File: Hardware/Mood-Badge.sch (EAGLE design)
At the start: 8 parts, among them U1 ATMEGA328P_TQFP

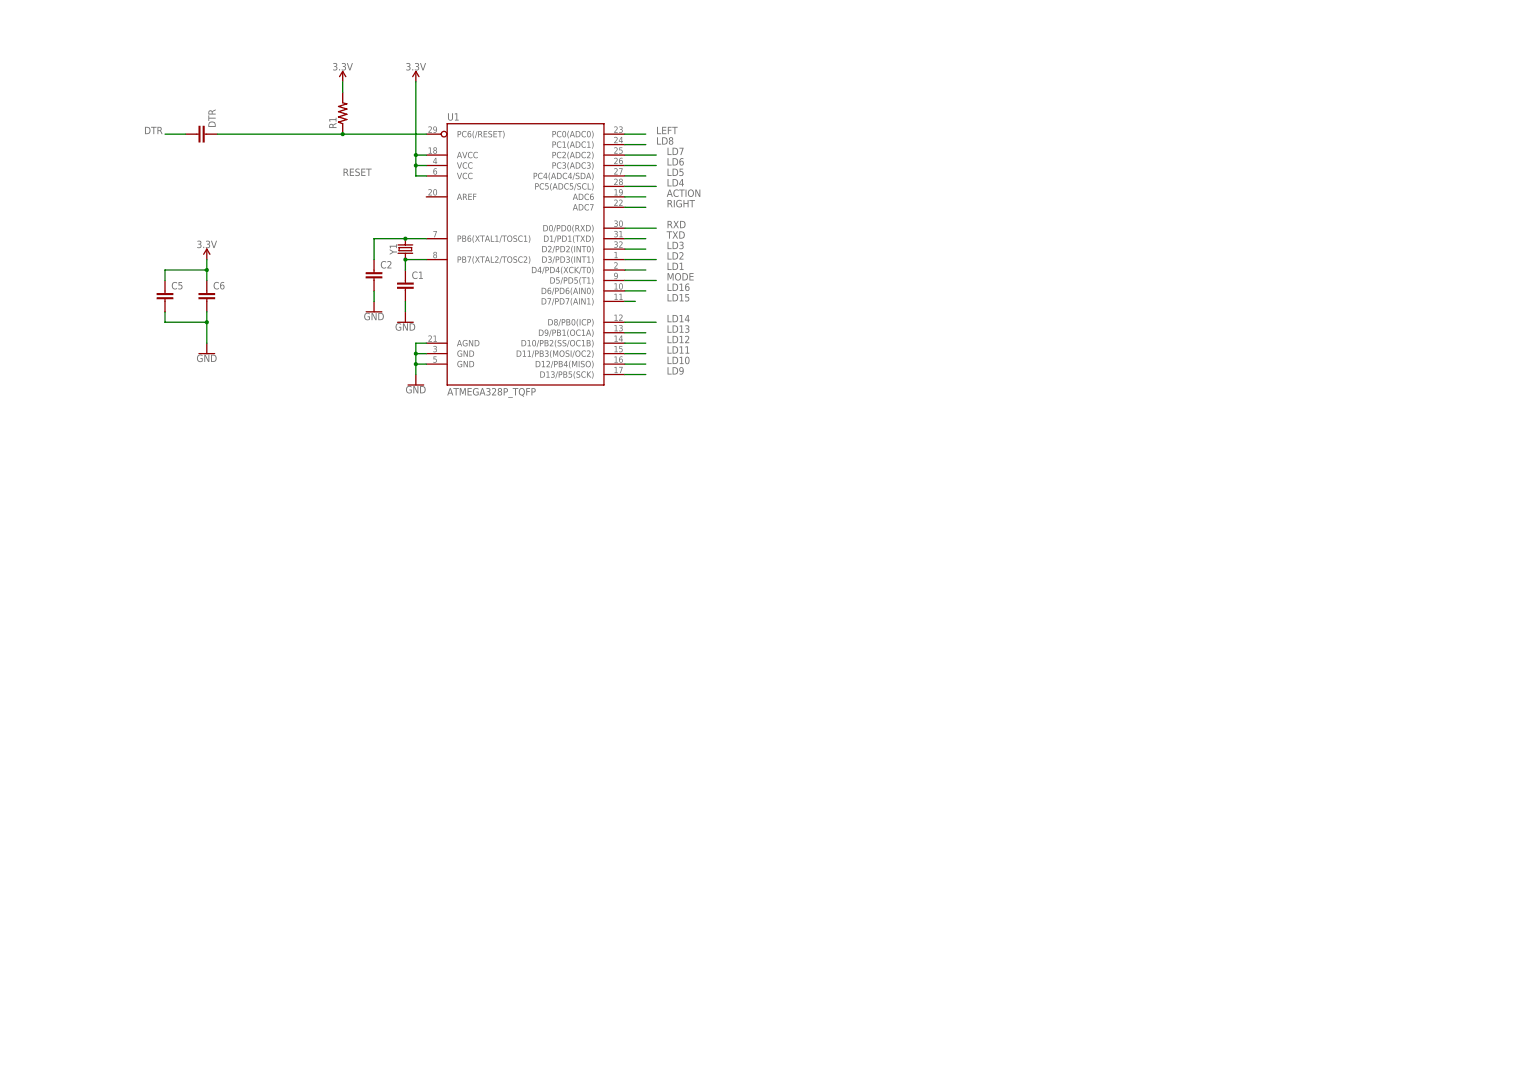
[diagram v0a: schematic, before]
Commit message: Power management circuit still in progress, bootload, ftdi, and LED matrix is done.
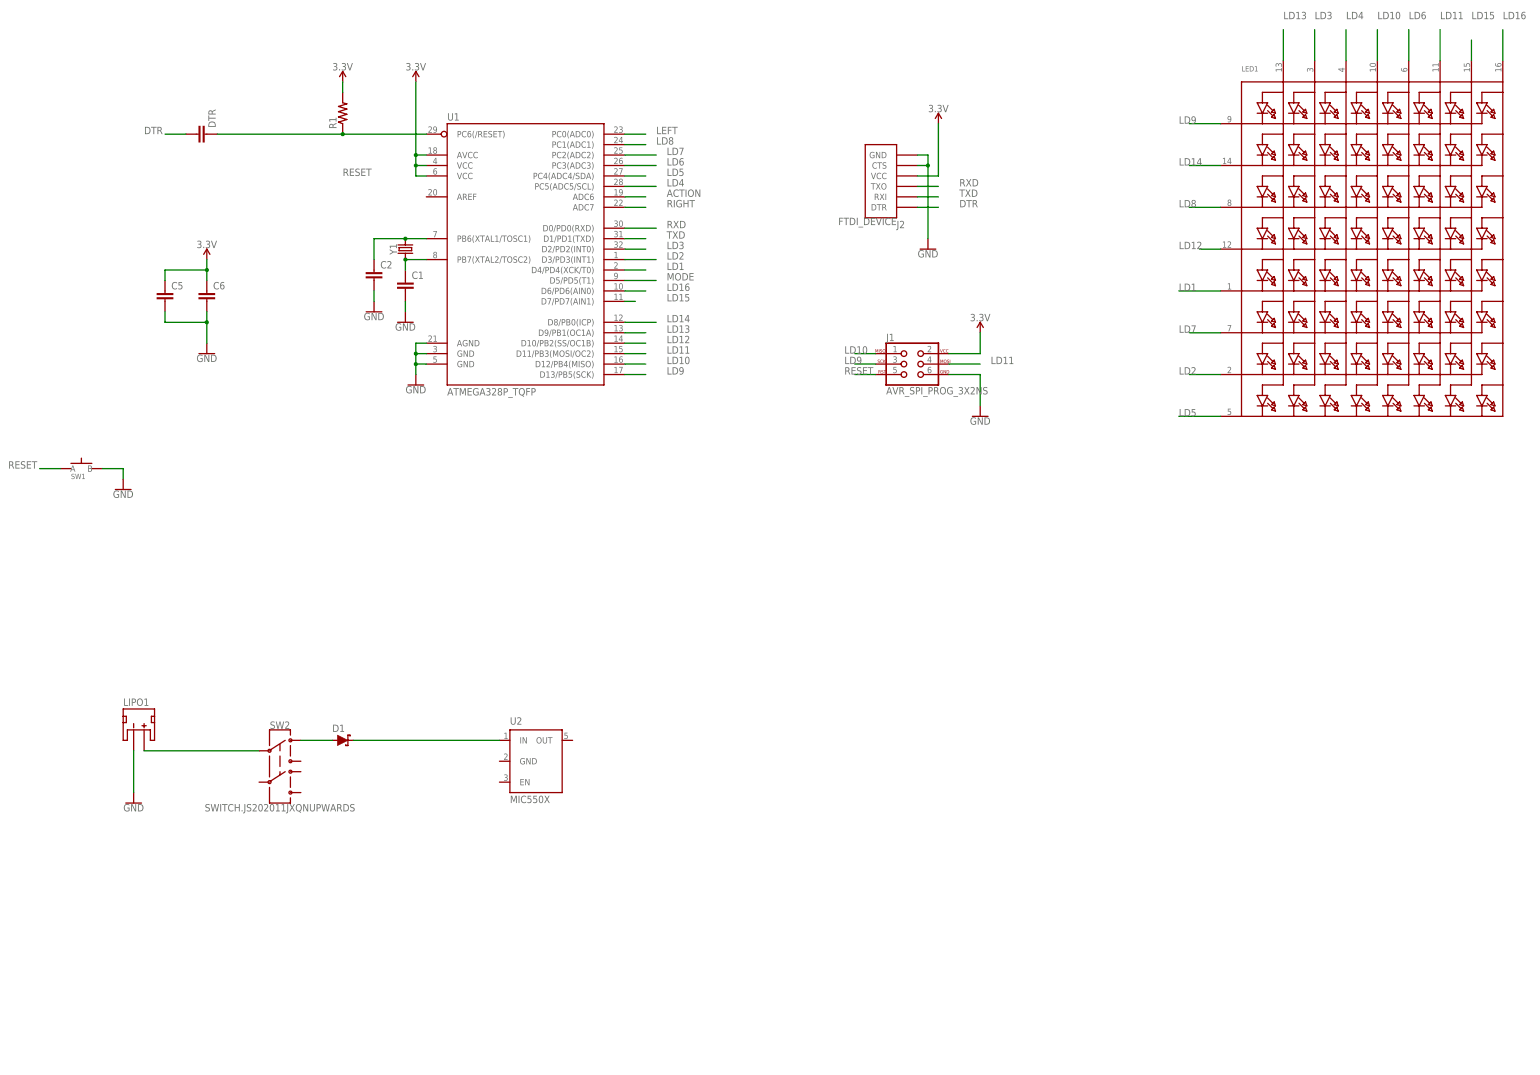
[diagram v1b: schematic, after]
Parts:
- added D1: (no value), LinnesLab-DiscreteSemi:SCHOTTKY-USC
- added J1: AVR_SPI_PROG_3X2NS, LinnesLab-Connectors:AVR_SPI_PROG_3X2NS
- added J2: FTDI_DEVICE, LinnesLab-Connectors:FTDI_DEVICE
- added LED1: (no value), LinnesLab-Displays:DOTMATRIX_8X8_ROWCATHODEM12A881UR
- added LIPO1: (no value), LinnesLab-Connectors:JST_2MM_MALE
- added SW1: (no value), LinnesLab-Switches:SPST.KT11P4SM34LFS
- added SW2: SWITCH.JS202011JXQNUPWARDS, LinnesLab-Switches:SWITCH.JS202011JXQNUPWARDS
- added U2: MIC550X, LinnesLab-Power:MIC550X
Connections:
- new net N$2: LIPO1.+, SW2.2
- new net N$3: D1.A, SW2.1
- new net N$5: D1.C, U2.IN
- net 3.3V: now also J1.2, J2.VCC
- net DTR: now also J2.DTR
- net GND: now also J1.6, J2.CTS, J2.GND, LIPO1.-, SW1.B
- net LD1: now also LED1.K5
- net LD10: now also J1.1, LED1.A4
- net LD11: now also J1.4, LED1.A6
- net LD12: now also LED1.K4
- net LD13: now also LED1.A1
- net LD14: now also LED1.K2
- net LD15: now also LED1.A7
- net LD16: now also LED1.A8
- net LD2: now also LED1.K7
- net LD3: now also LED1.A2
- net LD4: now also LED1.A3
- net LD5: now also LED1.K8
- net LD6: now also LED1.A5
- net LD7: now also LED1.K6
- net LD8: now also LED1.K3
- net LD9: now also J1.3, LED1.K1
- net RESET: now also J1.5, SW1.A
- net RXD: now also J2.TXO
- net TXD: now also J2.RXI

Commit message: day 3 changs
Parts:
- added C3, C4, C7: (no value), LinnesLab-Passives:CAPACITOR0603
- added D2: (no value), LinnesLab-DiscreteSemi:SCHOTTKY-USC
- added R2: (no value), LinnesLab-Passives:RESISTOR0603
- added U3: MCP73831.SOT23-5, LinnesLab-Power:MCP73831.SOT23-5
- added USB1: USB.MICRO-BIGGERPADS, LinnesLab-Connectors:USB.MICRO-BIGGERPADS
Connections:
- net N$2 renamed VLIPO
- removed net N$5: D1.C, U2.IN
- new net VIN: C3.1, C7.1, D1.C, D2.C, R2.2, U2.EN, U2.IN, U3.VIN
- new net V_USB: D2.A, USB1.V+
- net 3.3V: now also C4.1, U2.OUT
- net GND: now also C3.2, C4.2, C7.2, U2.GND, USB1.GND, USB1.SHIELD

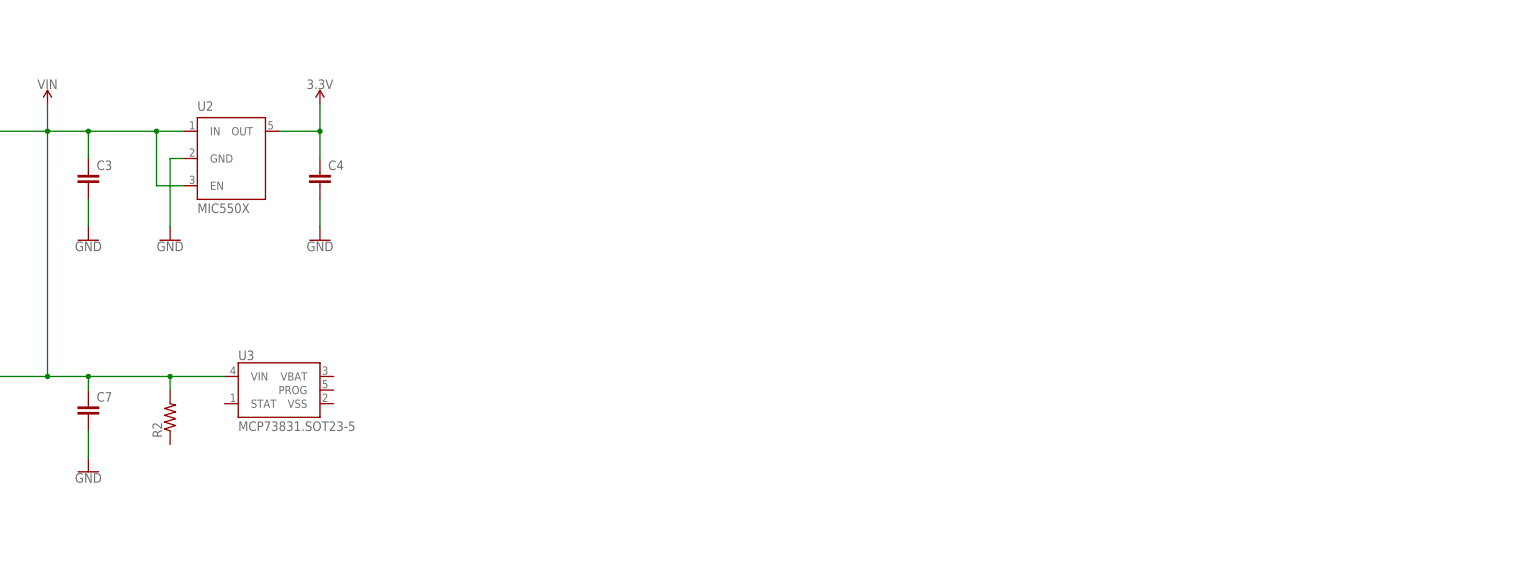
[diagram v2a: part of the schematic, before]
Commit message: the schematic is ready, the LED for the power managemnet circuit should still be added.
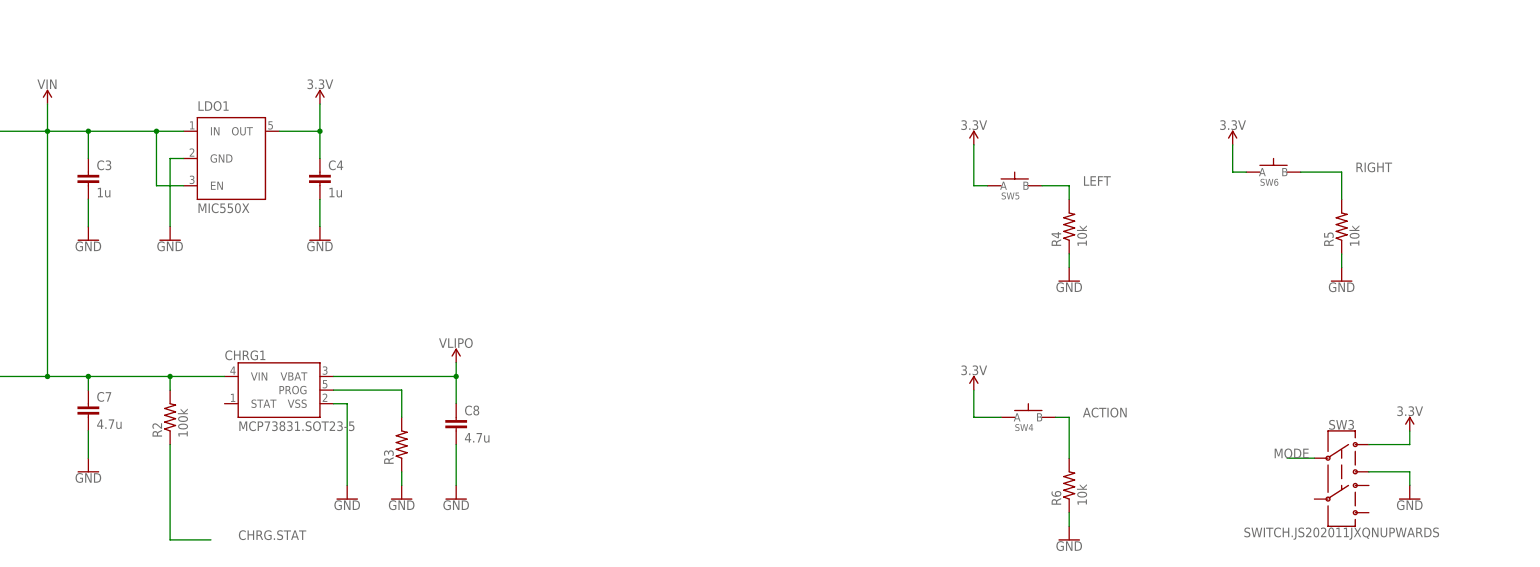
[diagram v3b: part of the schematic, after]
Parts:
- added C8: 4.7u, LinnesLab-Passives:CAPACITOR0603
- added R3: (no value), LinnesLab-Passives:RESISTOR0603
- added R4, R5, R6: 10k, LinnesLab-Passives:RESISTOR0603
- added SW3: SWITCH.JS202011JXQNUPWARDS, LinnesLab-Switches:SWITCH.JS202011JXQNUPWARDS
- added SW4, SW5, SW6: (no value), LinnesLab-Switches:SPST.KT11P4SM34LFS
- C3, C4: value (none) -> 1u
- C7: value (none) -> 4.7u
- R2: value (none) -> 100k
- renumbered U2 to LDO1, U3 to CHRG1
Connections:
- new net CHRG.STAT: R2.1
- new net N$5: CHRG1.PROG, R3.2
- net 3.3V: now also SW3.1, SW4.A, SW5.A, SW6.A
- net ACTION: now also R6.2, SW4.B
- net GND: now also C8.2, CHRG1.VSS, R3.1, R4.1, R5.1, R6.1, SW3.3
- net LEFT: now also R4.2, SW5.B
- net MODE: now also SW3.2
- net RIGHT: now also R5.2, SW6.B
- net VLIPO: now also C8.1, CHRG1.VBAT

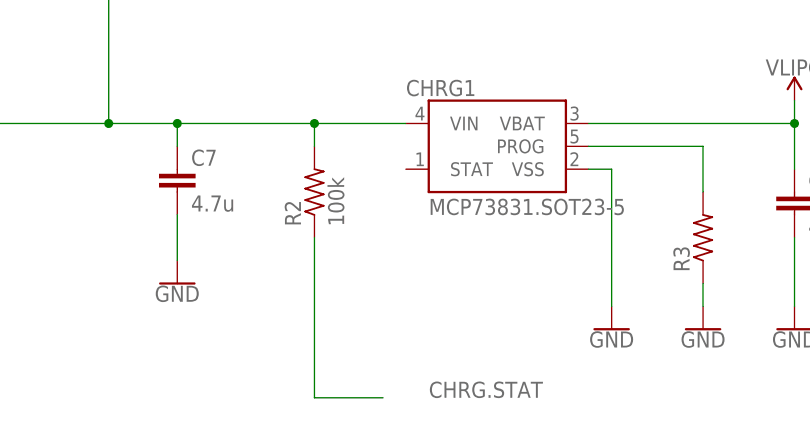
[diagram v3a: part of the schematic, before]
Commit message: added LED
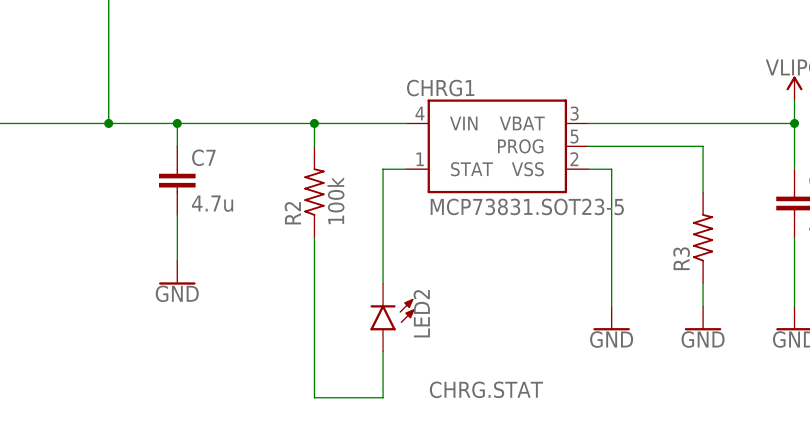
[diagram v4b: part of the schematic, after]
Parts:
- added LED2: (no value), LinnesLab-LED:LED0805
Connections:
- new net N$2: CHRG1.STAT, LED2.C
- net CHRG.STAT: now also LED2.A
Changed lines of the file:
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@@
 <layer number="146" name="DrillLegend_01-20" color="7" fill="1" visible="yes" active="yes"/>
 <layer number="147" name="PIN_NUMBER" color="7" fill="1" visible="yes" active="yes"/>
+<layer number="148" name="mDocument" color="7" fill="1" visible="yes" active="yes"/>
 <layer number="149" name="DrillLegend_02-15" color="7" fill="1" visible="yes" active="yes"/>
 <layer number="150" name="Notes" color="7" fill="1" visible="yes" active="yes"/>
@@
 <part name="SUPPLY14" library="LinnesLab-Symbols" deviceset="3.3V" device=""/>
 <part name="GND20" library="LinnesLab-Symbols" deviceset="GND" device=""/>
+<part name="LED2" library="LinnesLab-LED" deviceset="LED" device="0805"/>
 </parts>
 <sheets>
@@
 <instance part="GND20" gate="G$1" x="271.78" y="-116.84" smashed="yes">
 <attribute name="VALUE" x="271.78" y="-117.094" size="1.778" layer="96" align="top-center"/>
+</instance>
+<instance part="LED2" gate="G$1" x="48.26" y="-116.84" smashed="yes" rot="R180">
+<attribute name="NAME" x="51.689" y="-112.268" size="1.778" layer="95" font="vector" rot="R270"/>
+<attribute name="VALUE" x="46.355" y="-112.268" size="1.778" layer="96" font="vector" rot="R270" align="top-left"/>
 </instance>
 </instances>
@@
 <wire x1="40.64" y1="-124.46" x2="48.26" y2="-124.46" width="0.1524" layer="91"/>
 <label x="53.34" y="-124.46" size="1.778" layer="95"/>
+<pinref part="LED2" gate="G$1" pin="A"/>
+<wire x1="48.26" y1="-124.46" x2="48.26" y2="-119.38" width="0.1524" layer="91"/>
 </segment>
 </net>
@@
 </segment>
 </net>
+<net name="N$2" class="0">
+<segment>
+<pinref part="LED2" gate="G$1" pin="C"/>
+<wire x1="48.26" y1="-111.76" x2="48.26" y2="-99.06" width="0.1524" layer="91"/>
+<pinref part="CHRG1" gate="G$1" pin="STAT"/>
+<wire x1="48.26" y1="-99.06" x2="50.8" y2="-99.06" width="0.1524" layer="91"/>
+</segment>
+</net>
